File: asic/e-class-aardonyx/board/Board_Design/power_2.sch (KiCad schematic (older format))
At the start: 38 parts, among them Q1 FDN339AN, SW2 FSM2JSMAATR, U10 TPS7A7002DDAR, U11 ADM1085, U12 ADM1085, U13 TPS7A7002DDAR, U14 74AUP1G09GW

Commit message: add bom
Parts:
- C55, C59: Description CAP TANT 4.7UF 10% 16V 1206 -> CAP TANT 4.7UF 10% 16V 1206; Digikey PartNumber 399-3697-1-ND -> 399-18027-1-ND; Manufactured Part Number T491A475K016AT -> T491A475K016AT
- D4, D5: Maufaturer Lumex Opto/Components Inc. -> Lumex Opto/Components Inc.
- R45: Digikey PartNumber 311-4.7KJRTR-ND -> 311-4.7KJRCT-ND
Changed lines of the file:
@@
 F 1 "4.7UF,1206" V 1150 1300 50  0000 L CNN
 F 2 "Capacitor_SMD:C_1206_3216Metric" H 1300 1500 50  0001 C CNN
-F 3 "https://www.digikey.in/product-detail/en/kemet/T491A475K016AT/399-3697-1-ND/819022" H 1300 1500 50  0001 C CNN
-F 4 "	CAP TANT 4.7UF 10% 16V 1206" H 1300 1500 50  0001 C CNN "Description"
-F 5 "	399-3697-1-ND" H 1300 1500 50  0001 C CNN "Digikey PartNumber"
-F 6 "	T491A475K016AT" H 1300 1500 50  0001 C CNN "Manufactured Part Number"
+F 3 "https://www.digikey.in/product-detail/en/kemet/T491A475K016AT/399-18027-1-ND/819022" H 1300 1500 50  0001 C CNN
+F 4 "CAP TANT 4.7UF 10% 16V 1206" H 1300 1500 50  0001 C CNN "Description"
+F 5 "399-18027-1-ND" H 1300 1500 50  0001 C CNN "Digikey PartNumber"
+F 6 "T491A475K016AT" H 1300 1500 50  0001 C CNN "Manufactured Part Number"
 F 7 "Kemet" H 1300 1500 50  0001 C CNN "Maufaturer"
 	1    1300 1500
@@
 F 5 "67-1002-1-ND" H 5100 2000 50  0001 C CNN "Digikey PartNumber"
 F 6 "SML-LX1206GW-TR" H 5100 2000 50  0001 C CNN "Manufactured Part Number"
-F 7 "	Lumex Opto/Components Inc." H 5100 2000 50  0001 C CNN "Maufaturer"
+F 7 "Lumex Opto/Components Inc." H 5100 2000 50  0001 C CNN "Maufaturer"
 	1    5100 2000
 	0    -1   -1   0
@@
 F 1 "4.7UF,1206" H 6350 1650 50  0000 L CNN
 F 2 "Capacitor_SMD:C_1206_3216Metric" H 6300 1700 50  0001 C CNN
-F 3 "https://www.digikey.in/product-detail/en/kemet/T491A475K016AT/399-3697-1-ND/819022" H 6300 1700 50  0001 C CNN
-F 4 "	CAP TANT 4.7UF 10% 16V 1206" H 6300 1700 50  0001 C CNN "Description"
-F 5 "	399-3697-1-ND" H 6300 1700 50  0001 C CNN "Digikey PartNumber"
-F 6 "	T491A475K016AT" H 6300 1700 50  0001 C CNN "Manufactured Part Number"
+F 3 "https://www.digikey.in/product-detail/en/kemet/T491A475K016AT/399-18027-1-ND/819022" H 6300 1700 50  0001 C CNN
+F 4 "CAP TANT 4.7UF 10% 16V 1206" H 6300 1700 50  0001 C CNN "Description"
+F 5 "399-18027-1-ND" H 6300 1700 50  0001 C CNN "Digikey PartNumber"
+F 6 "T491A475K016AT" H 6300 1700 50  0001 C CNN "Manufactured Part Number"
 F 7 "Kemet" H 6300 1700 50  0001 C CNN "Maufaturer"
 	1    6300 1700
@@
 F 5 "67-1002-1-ND" H 10500 1800 50  0001 C CNN "Digikey PartNumber"
 F 6 "SML-LX1206GW-TR" H 10500 1800 50  0001 C CNN "Manufactured Part Number"
-F 7 "	Lumex Opto/Components Inc." H 10500 1800 50  0001 C CNN "Maufaturer"
+F 7 "Lumex Opto/Components Inc." H 10500 1800 50  0001 C CNN "Maufaturer"
 	1    10500 1800
 	0    -1   -1   0
@@
 F 1 "4.7KE, 0402" H 7150 4950 50  0000 L CNN
 F 2 "Resistor_SMD:R_0402_1005Metric" V 7140 4940 50  0001 C CNN
-F 3 "https://www.digikey.in/product-detail/en/yageo/RC0402JR-074K7L/311-4-7KJRTR-ND/726477" H 7100 4950 50  0001 C CNN
+F 3 "https://www.digikey.in/product-detail/en/yageo/RC0402JR-074K7L/311-4-7KJRCT-ND/726477" H 7100 4950 50  0001 C CNN
 F 4 "RES SMD 4.7K OHM 5% 1/16W 0402" H 7100 4950 50  0001 C CNN "Description"
-F 5 "311-4.7KJRTR-ND" H 7100 4950 50  0001 C CNN "Digikey PartNumber"
+F 5 "311-4.7KJRCT-ND" H 7100 4950 50  0001 C CNN "Digikey PartNumber"
 F 6 "RC0402JR-074K7L" H 7100 4950 50  0001 C CNN "Manufactured Part Number"
 F 7 "Yageo" H 7100 4950 50  0001 C CNN "Maufaturer"

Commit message: Updated few components
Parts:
- P_R44: Description RES SMD 120 OHM 1% 1/16W 0402 -> RES SMD 220 OHM 1% 1/16W 0402; Digikey PartNumber 311-120LRCT-ND -> 311-220LRDKR-ND; Manufactured Part Number RC0402FR-07120RL -> RC0402FR-07220RL
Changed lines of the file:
@@
 EESchema Schematic File Version 4
-EELAYER 30 0
+LIBS:Aardonyx-cache
+EELAYER 29 0
 EELAYER END
 $Descr A4 11693 8268
@@
 F 1 "220E,0402" H 5150 1500 50  0000 L CNN
 F 2 "Resistor_SMD:R_0402_1005Metric" V 5140 1540 50  0001 C CNN
-F 3 "https://www.digikey.in/product-detail/en/yageo/RC1206JR-07120RL/311-120ERCT-ND/732162" H 5100 1550 50  0001 C CNN
-F 4 "RES SMD 120 OHM 1% 1/16W 0402" H 5100 1550 50  0001 C CNN "Description"
-F 5 "311-120LRCT-ND" H 5100 1550 50  0001 C CNN "Digikey PartNumber"
-F 6 "RC0402FR-07120RL" H 5100 1550 50  0001 C CNN "Manufactured Part Number"
+F 3 "https://www.digikey.in/product-detail/en/yageo/RC0402FR-07220RL/311-220LRDKR-ND/732459" H 5100 1550 50  0001 C CNN
+F 4 "RES SMD 220 OHM 1% 1/16W 0402" H 5100 1550 50  0001 C CNN "Description"
+F 5 "311-220LRDKR-ND" H 5100 1550 50  0001 C CNN "Digikey PartNumber"
+F 6 "RC0402FR-07220RL" H 5100 1550 50  0001 C CNN "Manufactured Part Number"
 F 7 "Yageo" H 5100 1550 50  0001 C CNN "Maufaturer"
 	1    5100 1550

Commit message: Updating BOM
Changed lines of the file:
@@
 Wire Wire Line
 	3800 6700 3800 6750
-Text Label 3700 6500 0    50   ~ 0
-RESET_ASIC
 $Comp
 L Aardonyx-rescue:R_US-aardonyx R?
@@
 Wire Wire Line
 	7650 5250 8950 5250
-Wire Wire Line
-	3650 6500 4250 6500
 Text Label 7600 6200 0    50   ~ 0
 RESET_ASIC
@@
 	1    0    0    -1
 $EndComp
+Text Label 4300 6500 0    50   ~ 0
+RESET_ASIC
+Wire Wire Line
+	4300 6500 3650 6500
+Text Label 4200 4700 0    50   ~ 0
+V18_EN
 $EndSCHEMATC

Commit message: update footprint & bom
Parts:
- P_R39, P_R40: Description RES SMD 0 OHM JUMPER 1/8W 0805 -> RES SMD 0 OHM JUMPER 1/8W 0805; Manufactured Part Number CRCW08050000Z0EA -> CRCW08050000Z0EA
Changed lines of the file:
@@
 EESchema Schematic File Version 4
-LIBS:Aardonyx-cache
-EELAYER 29 0
+EELAYER 30 0
 EELAYER END
 $Descr A4 11693 8268
@@
 F 2 "Resistor_SMD:R_0805_2012Metric" V 2590 4790 50  0001 C CNN
 F 3 "https://www.digikey.com/product-detail/en/vishay-dale/CRCW08050000Z0EA/541-0-0ACT-ND/1180267" H 2550 4800 50  0001 C CNN
-F 4 " RES SMD 0 OHM JUMPER 1/8W 0805 " H 2550 4800 50  0001 C CNN "Description"
+F 4 "RES SMD 0 OHM JUMPER 1/8W 0805 " H 2550 4800 50  0001 C CNN "Description"
 F 5 " 541-0.0ACT-ND " H 2550 4800 50  0001 C CNN "Digikey PartNumber"
-F 6 " CRCW08050000Z0EA " H 2550 4800 50  0001 C CNN "Manufactured Part Number"
+F 6 "CRCW08050000Z0EA " H 2550 4800 50  0001 C CNN "Manufactured Part Number"
 F 7 "Vishay Dale" H 2550 4800 50  0001 C CNN "Maufaturer"
 	1    2550 4800
@@
 F 2 "Resistor_SMD:R_0805_2012Metric" V 2640 6590 50  0001 C CNN
 F 3 "https://www.digikey.com/product-detail/en/vishay-dale/CRCW08050000Z0EA/541-0-0ACT-ND/1180267" H 2600 6600 50  0001 C CNN
-F 4 " RES SMD 0 OHM JUMPER 1/8W 0805 " H 2600 6600 50  0001 C CNN "Description"
+F 4 "RES SMD 0 OHM JUMPER 1/8W 0805 " H 2600 6600 50  0001 C CNN "Description"
 F 5 " 541-0.0ACT-ND " H 2600 6600 50  0001 C CNN "Digikey PartNumber"
-F 6 " CRCW08050000Z0EA " H 2600 6600 50  0001 C CNN "Manufactured Part Number"
+F 6 "CRCW08050000Z0EA " H 2600 6600 50  0001 C CNN "Manufactured Part Number"
 F 7 "Vishay Dale" H 2600 6600 50  0001 C CNN "Maufaturer"
 	1    2600 6600

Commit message: Added few components
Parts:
- added C93, C94: 0.1UF,0402, Capacitor_SMD:C_0402_1005Metric, symbol Aardonyx-rescue:C_Small-aardonyx
- R48, R51, R55: value 10KE,0805 -> 10KE,0402; footprint Resistor_SMD:R_0805_2012Metric -> Resistor_SMD:R_0402_1005Metric; Description RES SMD 10K OHM 1% 1/8W 0805 -> RES 10K OHM 5% 1/8W 0402; Digikey PartNumber 311-10.0KCRCT-ND -> 2019-SG73S1ETTP103JCT-ND; Manufactured Part Number RC0805FR-0710KL -> SG73S1ETTP103J; Maufaturer Yageo -> KOA Speer Electronics, Inc.
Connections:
- net GND: now also C93.2, C94.2
- net V1P8: no longer C62.1
- net V3P3: now also C93.1, C94.1; no longer C56.1
- net at P_R1.2, P_R41.1, U10.6 (OUT): now also C56.1
- net at P_R2.2, P_R49.1, U13.6 (OUT): now also C62.1
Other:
- moved on the sheet: C56, C62, P_R1

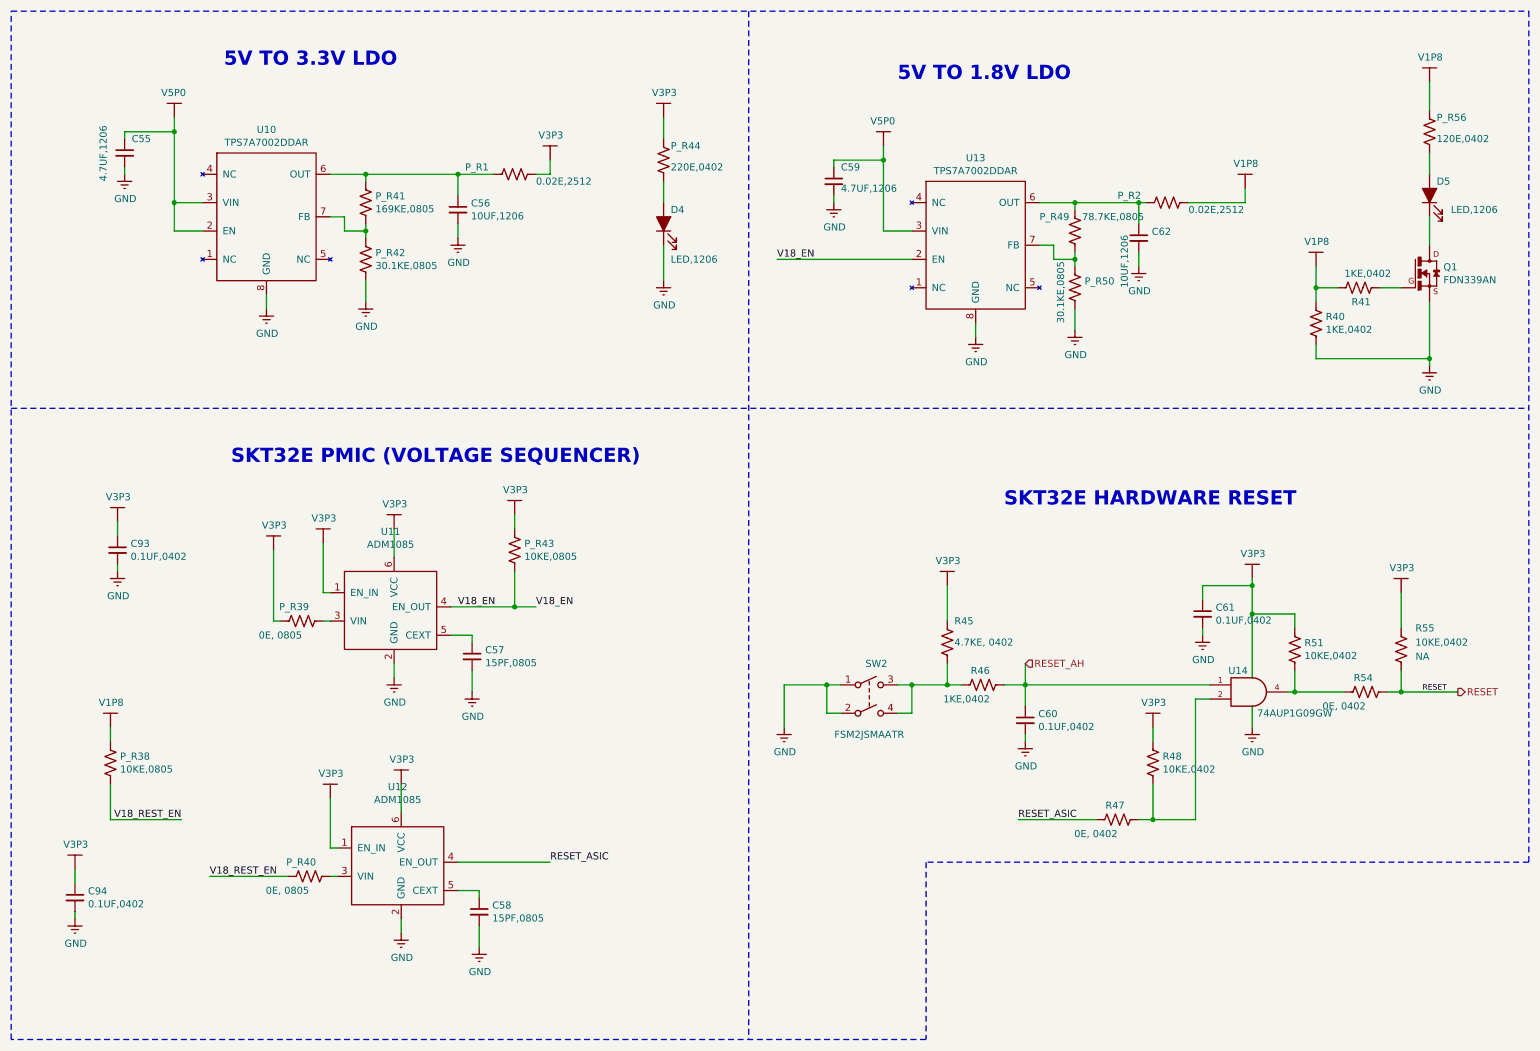
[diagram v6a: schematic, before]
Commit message: Replacing ADM1085 with ADM1186
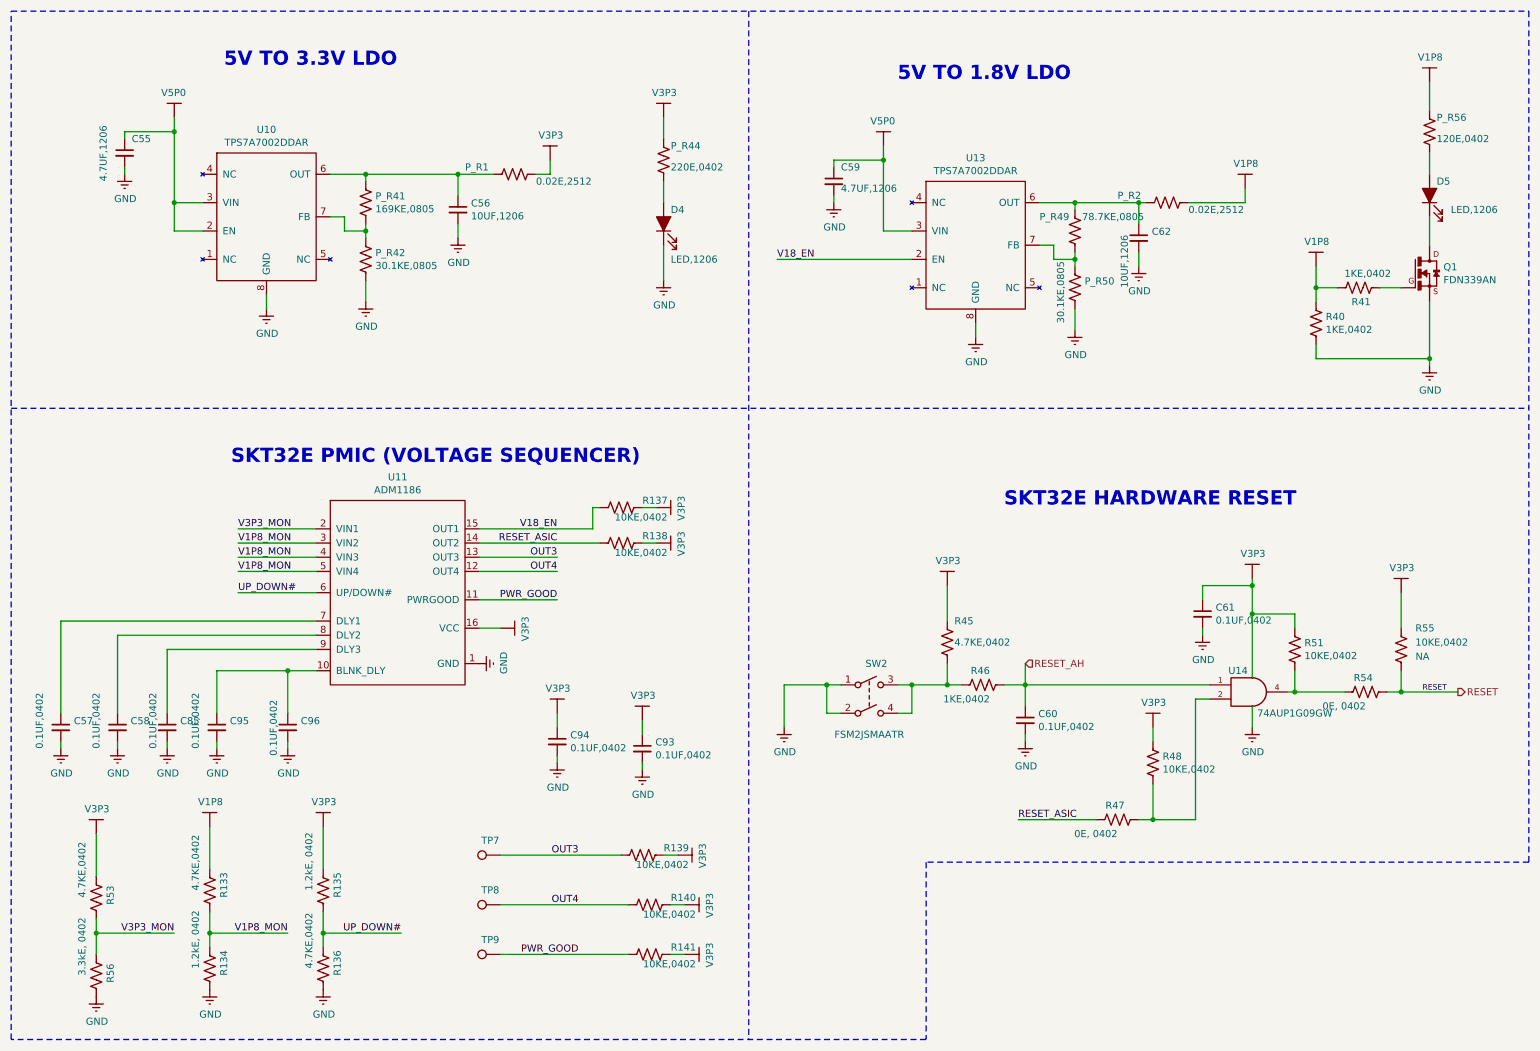
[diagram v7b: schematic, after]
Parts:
- removed P_R38, P_R43: 10KE,0805, Resistor_SMD:R_0805_2012Metric, symbol Aardonyx-rescue:R_US-aardonyx
- removed P_R39, P_R40: 0E, 0805, Resistor_SMD:R_0805_2012Metric, symbol Aardonyx-rescue:R_US-aardonyx
- removed U11, U12: ADM1085, Package_SO:SC-74-6_1.5x2.9mm_P0.95mm, symbol Aardonyx-rescue:ADM1085-skt32e_asic
- added C85, C95, C96: 0.1UF,0402, Capacitor_SMD:C_0402_1005Metric, symbol Aardonyx-rescue:C_Small-aardonyx
- added R133, R136, R53: 4.7KE,0402, Resistor_SMD:R_0402_1005Metric, symbol Aardonyx-rescue:R_US-aardonyx
- added R134, R135: 1.2kE, 0402, Resistor_SMD:R_0402_1005Metric, symbol Aardonyx-rescue:R_US-aardonyx
- added R137, R138, R139, R140, R141: 10KE,0402, Resistor_SMD:R_0402_1005Metric, symbol Aardonyx-rescue:R_US-aardonyx
- added R56: 3.3kE, 0402, Resistor_SMD:R_0402_1005Metric, symbol Aardonyx-rescue:R_US-aardonyx
- added TP7: OUT3, symbol Aardonyx-rescue:TestPoint-aardonyx
- added TP8: OUT4, symbol Aardonyx-rescue:TestPoint-aardonyx
- added TP9: POWER_GOOD, symbol Aardonyx-rescue:TestPoint-aardonyx
- added U11: ADM1186, symbol Aardonyx-rescue:ADM1186
- C57, C58: value 15PF,0805 -> 0.1UF,0402; footprint Capacitor_SMD:C_0805_2012Metric -> Capacitor_SMD:C_0402_1005Metric; Description CAP CER 15PF 25V C0G/NP0 0805 -> CAP CER 0.1UF 25V X7R 0402; Digikey PartNumber 732-7828-1-ND -> 478-10050-1-ND; Manufactured Part Number 885012007029 -> 04023C104JAT2A; Maufaturer Wurth Elektronik -> AVX Corporation
- R40, R41: footprint Resistor_SMD:R_0805_2012Metric -> Resistor_SMD:R_0402_1005Metric
- R45: value 4.7KE, 0402 -> 4.7KE,0402
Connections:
- net GND: now also C85.2, C95.2, C96.2, R134.2, R136.2, R56.2, U11.1 (GND)
- net RESET_ASIC: now also R138.2, U11.14 (OUT2)
- net V18_EN: now also R137.2, U11.15 (OUT1)
- net V1P8: now also R133.1
- net V3P3: now also R135.1, R137.1, R138.1, R139.1, R140.1, R141.1, R53.1, U11.16 (VCC)
- net at C57.1: now also U11.7 (DLY1)
- net at C58.1: now also U11.8 (DLY2)
- new net: C95.1, C96.1, U11.10 (BLNK_DLY)
- new net: C85.1, U11.9 (DLY3)
- new net OUT3: R139.2, TP7.1, U11.13 (OUT3)
- new net OUT4: R140.2, TP8.1, U11.12 (OUT4)
- new net PWR_GOOD: R141.2, TP9.1, U11.11 (PWRGOOD)
- new net UP_DOWN#: R135.2, R136.1, U11.6 (UP/DOWN#)
- new net V1P8_MON: R133.2, R134.1, U11.3 (VIN2), U11.4 (VIN3), U11.5 (VIN4)
- new net V3P3_MON: R53.2, R56.1, U11.2 (VIN1)
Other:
- moved on the sheet: C93, C94

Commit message: update change in footprint
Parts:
- TP7, TP8, TP9: footprint (none) -> Connector_PinHeader_2.54mm:PinHeader_1x01_P2.54mm_Vertical
- U11: footprint (none) -> Package_SO:QSOP-16_3.9x4.9mm_P0.635mm
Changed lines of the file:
@@
 F 0 "U11" H 3225 6015 50  0000 C CNN
 F 1 "ADM1186" H 3225 5924 50  0000 C CNN
-F 2 "" H 3200 4900 50  0001 C CNN
+F 2 "Package_SO:QSOP-16_3.9x4.9mm_P0.635mm" H 3200 4900 50  0001 C CNN
 F 3 "https://www.digikey.com/product-detail/en/analog-devices-inc/ADM1186-2ARQZ/ADM1186-2ARQZ-ND/1873703" H 3200 4900 50  0001 C CNN
 F 4 "Quad Sequencer 16QSOP" H 3200 4900 50  0001 C CNN "Description"
@@
 F 0 "TP7" V 4053 6522 50  0000 C CNN
 F 1 "OUT3" V 4054 6522 50  0001 C CNN
-F 2 "" H 4150 6450 50  0001 C CNN
+F 2 "Connector_PinHeader_2.54mm:PinHeader_1x01_P2.54mm_Vertical" H 4150 6450 50  0001 C CNN
 F 3 "" H 4150 6450 50  0001 C CNN
 	1    3950 6450
@@
 F 0 "TP8" V 4053 6872 50  0000 C CNN
 F 1 "OUT4" V 4054 6872 50  0001 C CNN
-F 2 "" H 4150 6800 50  0001 C CNN
+F 2 "Connector_PinHeader_2.54mm:PinHeader_1x01_P2.54mm_Vertical" H 4150 6800 50  0001 C CNN
 F 3 "" H 4150 6800 50  0001 C CNN
 	1    3950 6800
@@
 F 0 "TP9" V 4053 7222 50  0000 C CNN
 F 1 "POWER_GOOD" V 4054 7222 50  0001 C CNN
-F 2 "" H 4150 7150 50  0001 C CNN
+F 2 "Connector_PinHeader_2.54mm:PinHeader_1x01_P2.54mm_Vertical" H 4150 7150 50  0001 C CNN
 F 3 "" H 4150 7150 50  0001 C CNN
 	1    3950 7150
